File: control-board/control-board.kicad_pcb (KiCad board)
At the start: 2 copper layers, 0 parts

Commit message: control-board: update Ver 2025.9-1
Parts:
- added BZ1: Buzzer, Buzzer_Beeper:Buzzer_15x7.5RM7.6, F.Cu at (154.5, 140.8)
- added C1: 20p, Capacitor_SMD:C_0603_1608Metric, F.Cu at (185.9, 107.7)
- added C10: 100n, Capacitor_SMD:C_0603_1608Metric, F.Cu at (159.2, 115.5)
- added C11: 100n, Capacitor_SMD:C_0603_1608Metric, F.Cu at (176.6, 117.6)
- added C12: 20p, Capacitor_SMD:C_0603_1608Metric, F.Cu at (185.9, 112.9)
- added C13: 20p, Capacitor_SMD:C_0603_1608Metric, F.Cu at (189.9, 108.9)
- added C14: 100n, Capacitor_SMD:C_0603_1608Metric, F.Cu at (182.0, 102.5)
- added C15: 100n, Capacitor_SMD:C_0603_1608Metric, F.Cu at (182.0, 105.5)
- added C16: 1u, Capacitor_SMD:C_0603_1608Metric, F.Cu at (143.4, 120.1)
- added C17: 100n, Capacitor_SMD:C_0603_1608Metric, F.Cu at (157.9, 76.9)
- added C18: 100n, Capacitor_SMD:C_0603_1608Metric, F.Cu at (140.1, 76.9)
- added C19: 10u, Capacitor_SMD:C_0805_2012Metric, F.Cu at (134.1, 140.9)
- added C2: 20p, Capacitor_SMD:C_0603_1608Metric, F.Cu at (185.9, 103.4)
- added C20: 100n, Capacitor_SMD:C_0603_1608Metric, F.Cu at (157.9, 80.9)
- added C21: 1u, Capacitor_SMD:C_0603_1608Metric, F.Cu at (173.8, 142.3)
- added C22: 10u, Capacitor_SMD:C_0805_2012Metric, F.Cu at (131.0, 140.4)
- added C23: 1u, Capacitor_SMD:C_0603_1608Metric, F.Cu at (140.5, 86.7)
- added C24: 10u, Capacitor_SMD:C_0805_2012Metric, F.Cu at (169.8, 142.2)
- added C25: 100n, Capacitor_SMD:C_0603_1608Metric, F.Cu at (149.9, 117.6)
- added C26: 100n, Capacitor_SMD:C_0603_1608Metric, F.Cu at (157.4, 121.6)
- added C27: 100n, Capacitor_SMD:C_0603_1608Metric, F.Cu at (135.6, 134.4)
- added C28: 1u, Capacitor_SMD:C_0603_1608Metric, F.Cu at (126.7, 95.4)
- added C29: 1u, Capacitor_SMD:C_0603_1608Metric, F.Cu at (184.0, 142.4)
- added C3: 4u7, Capacitor_SMD:C_0805_2012Metric, F.Cu at (182.0, 99.5)
- added C30: 12p, Capacitor_SMD:C_0603_1608Metric, F.Cu at (128.6, 134.7)
- added C31: 22u, Capacitor_SMD:C_0805_2012Metric, F.Cu at (137.9, 140.9)
- added C32: 10u, Capacitor_SMD:C_0805_2012Metric, F.Cu at (180.1, 142.4)
- added C33: 22u, Capacitor_SMD:C_0805_2012Metric, F.Cu at (137.9, 143.2)
- added C34: 100n, Capacitor_SMD:C_0603_1608Metric, F.Cu at (130.7, 90.4)
- added C35: 100n, Capacitor_SMD:C_0603_1608Metric, F.Cu at (135.2, 90.4)
- added C4: 2u2, Capacitor_SMD:C_0805_2012Metric, F.Cu at (164.5, 96.2)
- added C5: 2u2, Capacitor_SMD:C_0805_2012Metric, F.Cu at (159.0, 112.8)
- added C6: 100n, Capacitor_SMD:C_0603_1608Metric, F.Cu at (178.0, 95.5)
- added C7: 100n, Capacitor_SMD:C_0603_1608Metric, F.Cu at (182.0, 110.7)
- added C8: 100n, Capacitor_SMD:C_0603_1608Metric, F.Cu at (175.0, 95.5)
- added C9: 100n, Capacitor_SMD:C_0603_1608Metric, F.Cu at (161.0, 96.7)
- added D1: LED, LED_SMD:LED_0805_2012Metric, F.Cu at (180.9, 87.4)
- added D2: LED, LED_SMD:LED_0805_2012Metric, F.Cu at (185.4, 87.4)
- added D3: LED, LED_SMD:LED_0805_2012Metric, F.Cu at (131.4, 105.1)
- added D4: LED, LED_SMD:LED_0805_2012Metric, F.Cu at (131.4, 108.6)
- added D5: LED, LED_SMD:LED_0805_2012Metric, F.Cu at (131.4, 111.8)
- added D6: LED, LED_SMD:LED_0805_2012Metric, F.Cu at (170.3, 128.4)
- added H1: MountingHole_Pad, MountingHole:MountingHole_3.2mm_M3_ISO14580_Pad, F.Cu at (123.0, 79.4)
- added H2: MountingHole_Pad, MountingHole:MountingHole_3.2mm_M3_ISO14580_Pad, F.Cu at (191.8, 79.4)
- added H3: MountingHole_Pad, MountingHole:MountingHole_3.2mm_M3_ISO14580_Pad, F.Cu at (191.8, 140.4)
- added H4: MountingHole_Pad, MountingHole:MountingHole_3.2mm_M3_ISO14580_Pad, F.Cu at (123.0, 140.4)
- added J1: Conn_01x03, Connector_PinHeader_2.54mm:PinHeader_1x03_P2.54mm_Vertical, F.Cu at (133.6, 122.9)
- added J10: DIN-4, M8_conn_panel:M8_Female_Conn_Panel_P4_90, F.Cu at (197.0, 84.5)
- added J11: DIN-4, M8_conn_panel:M8_Female_Conn_Panel_P4_90, F.Cu at (197.0, 119.5)
- added J12: Conn_01x03, Connector_PinHeader_2.54mm:PinHeader_1x03_P2.54mm_Vertical, F.Cu at (150.3, 98.8)
- added J13: Conn_01x03, Connector_PinHeader_2.54mm:PinHeader_1x03_P2.54mm_Vertical, F.Cu at (145.5, 110.6)
- added J2: GPS_ANT, Connector_Coaxial:SMA_Amphenol_901-143_Horizontal, F.Cu at (132.4, 78.5)
- added J3: LORA_ANT, Connector_Coaxial:SMA_Amphenol_901-143_Horizontal, F.Cu at (182.6, 78.5)
- added J4: DIN-4, M8_conn_panel:M8_Female_Conn_Panel_P4_90, F.Cu at (118.0, 85.0)
- added J5: DIN-4, M8_conn_panel:M8_Female_Conn_Panel_P4_90, F.Cu at (118.0, 136.3)
- added J6: USB_C_Receptacle_USB2.0_16P, Connector_USB:USB_C_Receptacle_HRO_TYPE-C-31-M-12, F.Cu at (114.0, 119.0)
- added J7: DIN-4, M8_conn_panel:M8_Female_Conn_Panel_P4_90, F.Cu at (118.0, 103.0)
- added J8: DIN-4, M8_conn_panel:M8_Female_Conn_Panel_P4_90, F.Cu at (197.0, 137.0)
- added J9: DIN-4, M8_conn_panel:M8_Female_Conn_Panel_P4_90, F.Cu at (197.0, 102.0)
- added JP1: Jumper_2_Open, Connector_PinHeader_2.54mm:PinHeader_1x02_P2.54mm_Vertical, F.Cu at (143.2, 124.1)
- added JP2: Jumper_2_Open, Connector_PinHeader_2.54mm:PinHeader_1x02_P2.54mm_Vertical, F.Cu at (124.5, 98.9)
- added L1: 22u, Inductor_SMD:L_0805_2012Metric, F.Cu at (139.1, 83.1)
- added L2: 15uH, Inductor_SMD:L_Coilcraft_XAL6060-XXX, F.Cu at (140.4, 135.9)
- added MOD1: WIRL-LORA_2618011181000, WIRL-LORA_2618011181000:WE-FP-8, F.Cu at (168.4, 82.9)
- added Q1: 2N7002, Package_TO_SOT_SMD:SOT-23, F.Cu at (163.5, 129.5)
- added R1: 10k, Resistor_SMD:R_0603_1608Metric, F.Cu at (173.6, 117.6)
- added R10: 150R, Resistor_SMD:R_0603_1608Metric, F.Cu at (195.2, 114.5)
- added R11: 150R, Resistor_SMD:R_0603_1608Metric, F.Cu at (194.6, 97.2)
- added R12: 150R, Resistor_SMD:R_0603_1608Metric, F.Cu at (194.6, 87.8)
- added R13: 5k1, Resistor_SMD:R_0603_1608Metric, F.Cu at (121.0, 115.5)
- added R14: 5k1, Resistor_SMD:R_0603_1608Metric, F.Cu at (121.0, 122.8)
- added R15: 10k, Resistor_SMD:R_0603_1608Metric, F.Cu at (136.2, 105.3)
- added R16: 10k, Resistor_SMD:R_0603_1608Metric, F.Cu at (136.2, 108.6)
- added R17: 10k, Resistor_SMD:R_0603_1608Metric, F.Cu at (136.2, 111.6)
- added R2: 60R, Resistor_SMD:R_0603_1608Metric, F.Cu at (140.4, 120.1)
- added R3: 60R, Resistor_SMD:R_0603_1608Metric, F.Cu at (146.4, 120.1)
- added R4: 22, Resistor_SMD:R_0603_1608Metric, F.Cu at (140.1, 80.3)
- added R5: 60R, Resistor_SMD:R_0603_1608Metric, F.Cu at (123.7, 94.4)
- added R6: 60R, Resistor_SMD:R_0603_1608Metric, F.Cu at (126.8, 92.5)
- added R7: 534k, Resistor_SMD:R_0603_1608Metric, F.Cu at (130.4, 136.9)
- added R8: 30k1, Resistor_SMD:R_0603_1608Metric, F.Cu at (131.9, 134.7)
- added R9: 10k, Resistor_SMD:R_0603_1608Metric, F.Cu at (173.8, 129.0)
- added SW1: SW_SPST, Button_Switch_SMD:SW_SPST_FSMSM, F.Cu at (181.6, 121.4)
- added TP1: TP_5V, TestPoint:TestPoint_THTPad_D1.5mm_Drill0.7mm, F.Cu at (183.6, 128.1)
- added TP2: TP_3V3, TestPoint:TestPoint_THTPad_D1.5mm_Drill0.7mm, F.Cu at (189.4, 128.1)
- added TP3: TP_15V, TestPoint:TestPoint_THTPad_D1.5mm_Drill0.7mm, F.Cu at (177.8, 128.1)
- added U1: STM32H743VITx, Package_QFP:LQFP-100_14x14mm_P0.5mm, F.Cu at (170.5, 106.7)
- added U2: NEO-XM, RF_GPS:ublox_NEO, F.Cu at (149.4, 82.9)
- added U3: SN65HVD256D, Package_SO:SOIC-8_3.9x4.9mm_P1.27mm, F.Cu at (151.9, 121.6)
- added U4: AMS1117-3.3, Package_TO_SOT_SMD:SOT-223-3_TabPin2, F.Cu at (172.0, 135.8)
- added U5: AP63200WU, Package_TO_SOT_SMD:TSOT-23-6, F.Cu at (134.4, 137.9)
- added U6: AMS1117-3.3, Package_TO_SOT_SMD:SOT-223-3_TabPin2, F.Cu at (182.0, 135.9)
- added U7: SN65HVD256D, Package_SO:SOIC-8_3.9x4.9mm_P1.27mm, F.Cu at (133.2, 95.4)
- added Y1: 8M, Crystal:Crystal_SMD_SeikoEpson_FA238-4Pin_3.2x2.5mm, F.Cu at (189.9, 104.9)
- added Y2: 32.768k, Crystal:Crystal_SMD_SeikoEpson_FA238-4Pin_3.2x2.5mm, F.Cu at (189.9, 113.4)
- added kibuzzard-68C81B55: G***, kibuzzard-68C81B55, F.Cu at (125.3, 108.6)
- added kibuzzard-68C81B65: G***, kibuzzard-68C81B65, F.Cu at (125.3, 105.1)
- added kibuzzard-68C81B7C: G***, kibuzzard-68C81B7C, F.Cu at (125.3, 111.8)
- added kibuzzard-68C81B8D: G***, kibuzzard-68C81B8D, F.Cu at (118.8, 103.0)
- added kibuzzard-68C81B8D: G***, kibuzzard-68C81B8D, F.Cu at (118.8, 85.0)
- added kibuzzard-68C81BE5: G***, kibuzzard-68C81BE5, F.Cu at (119.2, 131.4)
- added kibuzzard-68C81C0C: G***, kibuzzard-68C81C0C, F.Cu at (196.3, 102.0)
- added kibuzzard-68C81C5A: G***, kibuzzard-68C81C5A, F.Cu at (196.3, 119.5)
- added kibuzzard-68C81C70: G***, kibuzzard-68C81C70, F.Cu at (196.3, 84.4)
- added kibuzzard-68C831A8: G***, kibuzzard-68C831A8, F.Cu at (177.6, 125.2)
- added kibuzzard-68C831DA: G***, kibuzzard-68C831DA, F.Cu at (183.6, 125.2)
- added kibuzzard-68C831E3: G***, kibuzzard-68C831E3, F.Cu at (189.4, 125.2)
- added kibuzzard-68C836E4: G***, kibuzzard-68C836E4, F.Cu at (128.0, 117.8)
- added kibuzzard-68C836FB: G***, kibuzzard-68C836FB, F.Cu at (128.0, 120.5)
- added kibuzzard-68C839A7: G***, kibuzzard-68C839A7, F.Cu at (149.2, 93.0)
- added kibuzzard-68C839C6: G***, kibuzzard-68C839C6, F.Cu at (168.6, 93.0)
- added kibuzzard-68C8462F: G***, kibuzzard-68C8462F, F.Cu at (196.2, 133.2)
- added kibuzzard-68C84A93: G***, kibuzzard-68C84A93, F.Cu at (187.2, 92.6)
- added kibuzzard-68CAD58E: G***, kibuzzard-68CAD58E, F.Cu at (147.8, 101.6)
- added kibuzzard-68CAD5A3: G***, kibuzzard-68CAD5A3, F.Cu at (148.0, 107.8)
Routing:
- net +3V3: track 0.00 -> 277.1 mm, vias 0 -> 8
- net VDC: track 0.00 -> 206.8 mm, vias 0 -> 7
- net +5V: track 0.00 -> 121.5 mm, vias 0 -> 4
- net CAN1_N: track 0.00 -> 121.1 mm, vias 0 -> 1
- net CAN1_P: track 0.00 -> 114.6 mm, vias 0 -> 1
- net GND: track 0.00 -> 90.4 mm, vias 0 -> 31
- net +15V: track 0.00 -> 76.9 mm, vias 0 -> 2
- net CAN2_N: track 0.00 -> 54.4 mm
- net DP: track 0.00 -> 51.0 mm
- net DN: track 0.00 -> 50.9 mm
- net CAN2_P: track 0.00 -> 47.9 mm
- net ADC_APPS1: track 0.00 -> 46.6 mm
- net Net-(D2-A): track 0.00 -> 39.3 mm, vias 0 -> 2
- net ADC_BPPS: track 0.00 -> 38.6 mm, vias 0 -> 2
- net ADC_APPS2: track 0.00 -> 37.8 mm, vias 0 -> 2
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- added copper zone on F.Cu, net +15V
- added copper zone on B.Cu, net GND
- added copper zone on F.Cu, net GND
- added copper zone on F.Cu, net Net-(U5-FB)
- added copper zone on F.Cu, net Net-(U5-SW)
- added copper zone on B.Cu, net VDC
- added copper zone on F.Cu, net VDC
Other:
- board outline added: 94.9 x 73 mm
- board text added: "+"
- board text added: "-"
- board text added: "1"

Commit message: modify: control board
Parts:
- removed C19, C22: 10u, Capacitor_SMD:C_0805_2012Metric
- removed C27: 100n, Capacitor_SMD:C_0603_1608Metric
- removed C30: 12p, Capacitor_SMD:C_0603_1608Metric
- removed C31, C33: 22u, Capacitor_SMD:C_0805_2012Metric
- removed L2: 15uH, Inductor_SMD:L_Coilcraft_XAL6060-XXX
- removed R8: 30k1, Resistor_SMD:R_0603_1608Metric
- removed U5: AP63200WU, Package_TO_SOT_SMD:TSOT-23-6
- removed the kibuzzard-68C81B8D at (118.8, 103.0)
- added D7: LED, LED_SMD:LED_0805_2012Metric, F.Cu at (127.4, 121.5)
- added D8: BAT46, Diode_THT:D_DO-35_SOD27_P7.62mm_Horizontal, F.Cu at (118.8, 103.8)
- added J14: Conn_01x02, Connector_PinHeader_2.54mm:PinHeader_1x02_P2.54mm_Vertical, F.Cu at (113.6, 104.2)
- added J15: Conn_01x03, Connector_JST:JST_EH_B3B-EH-A_1x03_P2.50mm_Vertical, F.Cu at (177.2, 140.7)
- added Q2: 2N7002, Package_TO_SOT_SMD:SOT-23, F.Cu at (131.4, 122.5)
- added kibuzzard-68DAC17B: G***, kibuzzard-68DAC17B, F.Cu at (113.6, 101.6)
- added kibuzzard-68DAC5A1: G***, kibuzzard-68DAC5A1, F.Cu at (155.1, 135.2)
- added kibuzzard-68DAC5B3: G***, kibuzzard-68DAC5B3, F.Cu at (130.2, 96.2)
- J7: value DIN-4 -> Conn_01x03; footprint M8_conn_panel:M8_Female_Conn_Panel_P4_90 -> Connector_JST:JST_EH_B3B-EH-A_1x03_P2.50mm_Vertical
- R7: value 534k -> 10k
- moved J7 59.3 mm to (163.8, 140.7), turned to 0 degrees
- moved C29 29.7 mm to (159.2, 126.0), turned to 90 degrees
- moved C32 29.1 mm to (159.2, 122.0), turned to 90 degrees
- moved Q1 22.5 mm to (142.7, 121.0)
- moved R2 20.4 mm to (148.2, 139.0), turned to 180 degrees
- moved U6 20.1 mm to (165.8, 124.0), turned to 0 degrees
- moved BZ1 19.0 mm to (135.7, 137.8)
- moved D6 17.4 mm to (187.0, 133.6), turned to -90 degrees
- moved C16 16.6 mm to (148.2, 136.0), turned to 0 degrees
- moved C21 16.3 mm to (159.2, 135.0), turned to 90 degrees
- moved C24 15.3 mm to (159.3, 131.0), turned to 90 degrees
- moved JP1 15.2 mm to (152.2, 136.3), turned to 180 degrees
- moved R3 13.0 mm to (148.2, 133.0), turned to 180 degrees
- moved C25 12.6 mm to (145.8, 129.5), turned to 90 degrees
- moved R7 12.3 mm to (127.4, 125.0), turned to 180 degrees
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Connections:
- J10 pad 1: VDC -> +15V
- J10 pad 3: ADC_BPPS -> ADC_STEER
- J11 pad 1: VDC -> +15V
- J4 pad 1: VDC -> +15V
- J6 pad A4: unconnected-(J6-VBUS-PadA4) -> Net-(D8-A)
- J6 pad A9: unconnected-(J6-VBUS-PadA4) -> Net-(D8-A)
- J6 pad B4: unconnected-(J6-VBUS-PadA4) -> Net-(D8-A)
- J6 pad B9: unconnected-(J6-VBUS-PadA4) -> Net-(D8-A)
- J7 pad 1: VDC -> +15V
- J7 pad 2: CAN2_P -> GPIO7
- J7 pad 3: CAN2_N -> GND
- J9 pad 1: VDC -> +15V
- R7 pad 1: +15V -> +3V3
- R9 pad 1: +15V -> +3V3
- U1 pad 32: ADC_BPPS -> unconnected-(U1-PC4-Pad32)
- U1 pad 33: unconnected-(U1-PC5-Pad33) -> ADC_BPPS
- U1 pad 35: unconnected-(U1-PB1-Pad35) -> ADC_STEER
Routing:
- net +15V: track 76.9 -> 288.2 mm, vias 2 -> 3
- net VDC: track 206.8 -> 111.0 mm, vias 7 -> 0
- net CAN2_N: track 54.4 -> 18.9 mm
- net ADC_STEER: track 0.00 -> 35.4 mm
- net +3V3: track 277.1 -> 309.7 mm, vias 8 -> 9
- net GPIO8: track 0.00 -> 31.0 mm, vias 0 -> 1
- net CAN2_P: track 47.9 -> 19.6 mm
- net GPIO7: track 0.00 -> 27.0 mm, vias 0 -> 1
- net Net-(D8-A): track 0.00 -> 17.5 mm
- net CAN1_N: track 121.1 -> 107.3 mm
- net BUZZ: track 35.0 -> 48.1 mm
- net CAN1_RX: track 15.3 -> 26.8 mm
- net unconnected-(J6-VBUS-PadA4): track 9.48 -> 0.00 mm
- net Net-(D7-K): track 0.00 -> 9.47 mm
- net GND: track 90.4 -> 81.6 mm, vias 31 -> 21
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- added copper zone on B.Cu, net +15V
- removed copper zone on F.Cu, net Net-(D7-A)
- removed copper zone on F.Cu, net Net-(U5-SW)
- removed copper zone on B.Cu, net VDC
- removed copper zone on F.Cu, net VDC

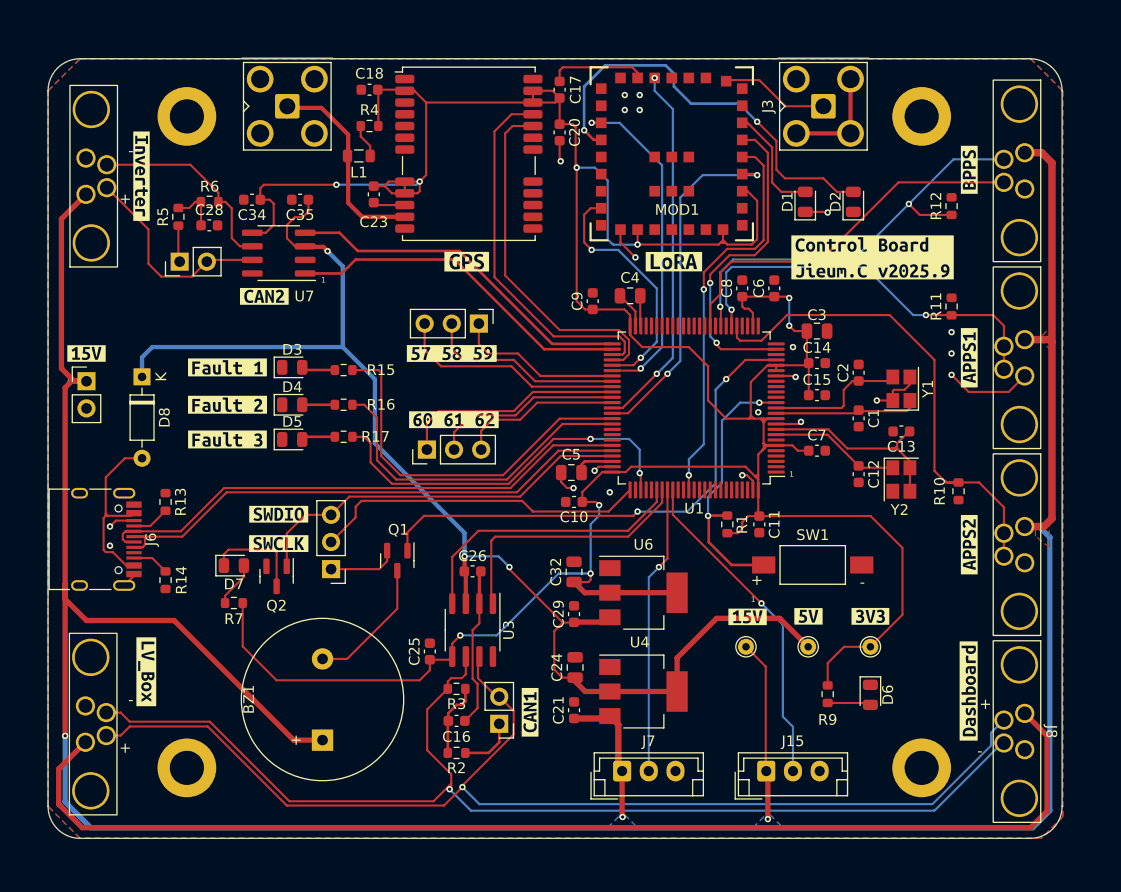
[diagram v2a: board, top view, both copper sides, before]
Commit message: modify: diodes and JST footprint
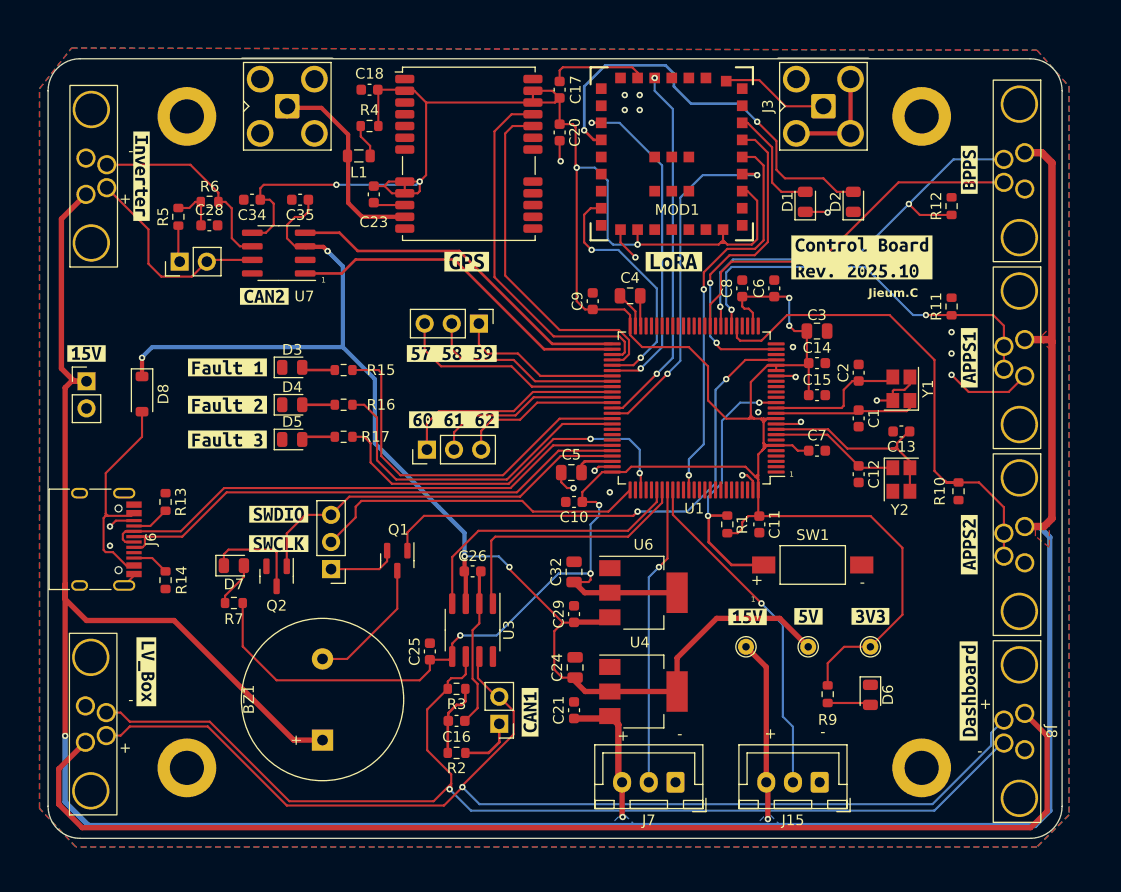
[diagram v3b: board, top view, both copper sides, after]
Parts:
- removed kibuzzard-68C84A93: G***, kibuzzard-68C84A93
- added kibuzzard-68E0D157: G***, kibuzzard-68E0D157, F.Cu at (186.2, 92.6)
- D8: footprint Diode_THT:D_DO-35_SOD27_P7.62mm_Horizontal -> Diode_SMD:D_SOD-123
- J15, J7: footprint Connector_JST:JST_EH_B3B-EH-A_1x03_P2.50mm_Vertical -> Connector_JST:JST_XH_B3B-XH-A_1x03_P2.50mm_Vertical
- moved J15 5.11 mm to (182.2, 141.8), turned to 180 degrees
- moved J7 5.11 mm to (168.8, 141.8), turned to 180 degrees
- moved D8 1.61 mm to (118.8, 105.4)
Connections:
- J15 pad 1: +15V -> GND
- J15 pad 3: GND -> +15V
- J7 pad 1: +15V -> GND
- J7 pad 3: GND -> +15V
- U1 pad 85: GPIO9 -> unconnected-(U1-PD4-Pad85)
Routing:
- net Net-(D8-A): track 17.5 -> 20.9 mm
- net +15V: track 288.2 -> 286.4 mm
- net +5V: vias 3 -> 4
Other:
- board text added: "Jieum.C"

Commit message: modify: add 5V power
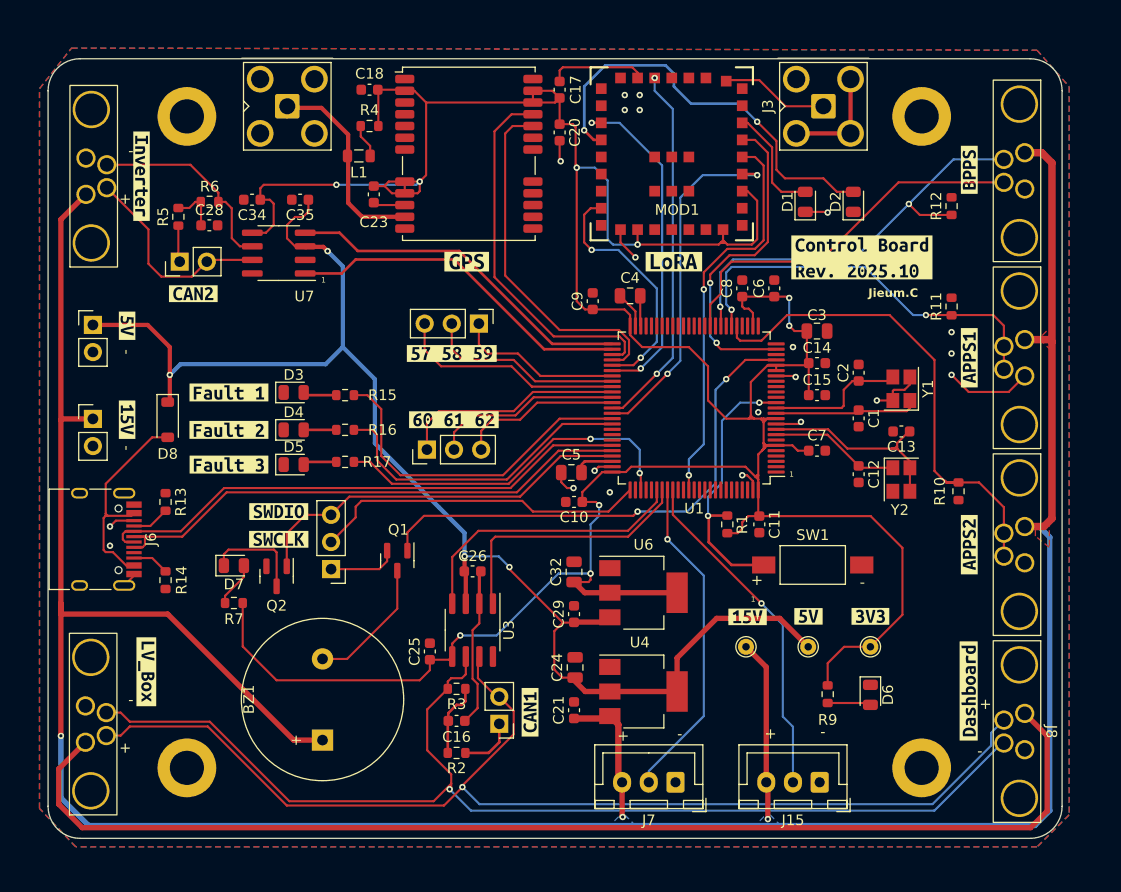
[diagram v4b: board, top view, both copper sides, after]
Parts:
- added J16: Conn_01x02, Connector_PinHeader_2.54mm:PinHeader_1x02_P2.54mm_Vertical, F.Cu at (114.2, 98.9)
- added kibuzzard-68E0D6FC: G***, kibuzzard-68E0D6FC, F.Cu at (117.4, 99.0)
- moved kibuzzard-68DAC17B 7.27 mm to (117.4, 107.8), turned to -90 degrees
- moved kibuzzard-68DAC5B3 6.65 mm to (123.6, 96.0)
- moved J14 3.58 mm to (114.2, 107.7)
- moved D8 3.39 mm to (121.2, 107.8)
- moved kibuzzard-68C81B55 2.35 mm to (126.9, 108.8)
- moved kibuzzard-68C81B65 2.35 mm to (126.9, 105.2)
- moved kibuzzard-68C81B7C 2.35 mm to (126.9, 112.0)
- moved D3 2.35 mm to (133.0, 105.2)
- moved D4 2.35 mm to (133.0, 108.8)
- moved D5 2.35 mm to (133.0, 112.0)
- moved R15 2.35 mm to (137.8, 105.5)
- moved R16 2.35 mm to (137.8, 108.8)
- moved R17 2.35 mm to (137.8, 111.8)
- moved kibuzzard-68C836FB 0.40 mm to (131.6, 119.0)
- moved kibuzzard-68C836E4 0.25 mm to (131.6, 116.4)
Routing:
- net +5V: track 120.1 -> 129.7 mm
- net GPIO7: track 27.0 -> 30.9 mm
- net Fault1: track 35.2 -> 32.1 mm
- net Fault3: track 35.7 -> 33.6 mm
- net Fault2: track 31.7 -> 29.7 mm
- net +15V: track 286.4 -> 285.7 mm
- net Net-(D8-A): track 20.9 -> 20.4 mm

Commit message: v2025.10
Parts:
- added D9: LED, LED_SMD:LED_0805_2012Metric, F.Cu at (123.5, 100.1)
- added J17: Conn_01x02, Connector_PinHeader_2.54mm:PinHeader_1x02_P2.54mm_Vertical, F.Cu at (156.5, 141.2)
- added J18: Conn_01x02, Connector_PinHeader_2.54mm:PinHeader_1x02_P2.54mm_Vertical, F.Cu at (133.0, 98.8)
- added R8: 10k, Resistor_SMD:R_0603_1608Metric, F.Cu at (120.2, 99.0)
- added kibuzzard-68E0D6FC: G***, kibuzzard-68E0D6FC, F.Cu at (126.0, 100.0)
- Q2: value 2N7002 -> NXV90EPR
- U3, U7: value SN65HVD256D -> TCAN1462VDRQ1
- moved R7 4.21 mm to (127.5, 120.8)
- moved D7 2.04 mm to (127.5, 123.5), turned to 180 degrees
- moved Q2 1.25 mm to (132.0, 123.6)
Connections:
- D7 pad 1: Net-(D7-K) -> GND
- Q2 pad 1: SWDIO -> Net-(Q2-D)
- Q2 pad 2: GND -> NRST
- Q2 pad 3: Net-(D7-K) -> +3V3
- R1 pad 2: Net-(SW1-B) -> NRST
- R7 pad 1: +3V3 -> Net-(Q2-D)
- SW1 pad 2: Net-(SW1-B) -> NRST
- U1 pad 14: Net-(SW1-B) -> NRST
- U3 pad 8: unconnected-(U3-S-Pad8) -> GND
- U7 pad 8: unconnected-(U7-S-Pad8) -> GND
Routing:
- net NRST: track 0.00 -> 80.2 mm, vias 0 -> 3
- net Net-(SW1-B): track 25.5 -> 0.00 mm, vias 2 -> 0
- net CAN1_N: track 107.3 -> 117.9 mm
- net Net-(D7-K): track 9.47 -> 0.00 mm
- net CAN2_N: track 18.9 -> 27.9 mm
- net CAN2_P: track 19.6 -> 27.7 mm
- net SWDIO: track 36.6 -> 28.6 mm
- net CAN1_P: track 108.6 -> 114.2 mm
- net Net-(Q2-D): track 0.00 -> 5.40 mm
- net +3V3: track 309.7 -> 306.9 mm
- net Net-(D9-A): track 0.00 -> 2.48 mm
- net Net-(D7-A): track 4.23 -> 2.80 mm
- net GND: vias 21 -> 461
